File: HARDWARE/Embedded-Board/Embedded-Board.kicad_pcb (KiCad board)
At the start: 2 copper layers, 80 x 60 mm, 81 parts, among them J1 AD7265X, J11 USB_C_Receptacle_USB2.0, J2 POWER-pins, J3 Conn_02x20_Odd_Even, J4 AD7341, J5 I2C comm, J6 GPIO PINS, Q1 MMUN2133LT1G, SW1 SW_Push, SW2 RotaryEncoder_Switch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

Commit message: small update
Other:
- board text added: "Harvey McBurney Ryan Najami Nicolas Viale"
- board text removed: "Harvet McBurney Ryan Namaji Nicolas Viale"

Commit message: Final PCB version
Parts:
- added D4: WHITE-LED, LED_SMD:LED_1206_3216Metric, F.Cu at (173.2, 88.6)
- added D5: IR_LED, LED_SMD:LED_0805_2012Metric, F.Cu at (187.1, 88.6)
- added D6: UV_LED, LED_SMD:LED_PLCC_2835, F.Cu at (180.2, 76.7)
- added G***: LOGO, test:uofg-8mm, B.Cu at (180.2, 84.7)
- added J7: BOARD->LED, Connector_PinHeader_2.54mm:PinHeader_1x03_P2.54mm_Vertical, F.Cu at (152.8, 68.4)
- added J8: LED->BOARD, Connector_PinHeader_2.54mm:PinHeader_1x03_P2.54mm_Vertical, F.Cu at (203.4, 68.4)
- added JP1: VBUS-5V, Jumper:SolderJumper-2_P1.3mm_Open_TrianglePad1.0x1.5mm, F.Cu at (84.3, 96.7)
- added JP2: OUT-5V, Jumper:SolderJumper-2_P1.3mm_Bridged_Pad1.0x1.5mm, F.Cu at (110.8, 100.2)
- added Q3: Q_NPN_BEC, Package_TO_SOT_THT:TO-92_Wide, B.Cu at (169.9, 95.6)
- added Q4: Q_NPN_BEC, Package_TO_SOT_THT:TO-92_Wide, B.Cu at (184.8, 95.9)
- added Q5: Q_NPN_BEC, Package_TO_SOT_THT:TO-92_Wide, B.Cu at (182.7, 71.4)
- added R23: 10k, Resistor_THT:R_Axial_DIN0411_L9.9mm_D3.6mm_P12.70mm_Horizontal, B.Cu at (186.6, 102.9)
- added R24: 10k, Resistor_THT:R_Axial_DIN0411_L9.9mm_D3.6mm_P12.70mm_Horizontal, B.Cu at (198.4, 91.7)
- added R25: 10k, Resistor_THT:R_Axial_DIN0411_L9.9mm_D3.6mm_P12.70mm_Horizontal, B.Cu at (192.8, 59.4)
- added R26: 470, Resistor_THT:R_Axial_DIN0411_L9.9mm_D3.6mm_P12.70mm_Horizontal, B.Cu at (165.2, 110.9)
- added R27: 470, Resistor_THT:R_Axial_DIN0411_L9.9mm_D3.6mm_P12.70mm_Horizontal, B.Cu at (194.6, 111.2)
- added R28: 470, Resistor_THT:R_Axial_DIN0411_L9.9mm_D3.6mm_P12.70mm_Horizontal, B.Cu at (172.3, 59.0)
- added REF**: Fiducial_1mm_Mask3mm, Fiducial:Fiducial_1mm_Mask3mm, F.Cu at (197.1, 116.6)
- added REF**: TestPoint, user:1.3mm_Test_Point, F.Cu at (202.2, 51.6)
- added REF**: Fiducial_1mm_Mask3mm, Fiducial:Fiducial_1mm_Mask3mm, F.Cu at (83.2, 52.7)
- added REF**: MountingHole_3.2mm_M3_ISO14580_Pad, MountingHole:MountingHole_3.2mm_M3_ISO14580_Pad, F.Cu at (185.2, 62.1)
- added REF**: TestPoint, user:1.3mm_Test_Point, F.Cu at (202.1, 117.7)
- added REF**: MountingHole_3.2mm_M3_ISO14580_Pad, MountingHole:MountingHole_3.2mm_M3_ISO14580_Pad, F.Cu at (135.2, 62.1)
- added REF**: MountingHole_3.2mm_M3_ISO14580_Pad, MountingHole:MountingHole_3.2mm_M3_ISO14580_Pad, F.Cu at (163.8, 92.2)
- added REF**: TestPoint, user:1.3mm_Test_Point, F.Cu at (78.2, 51.6)
- added REF**: Fiducial_1mm_Mask3mm, Fiducial:Fiducial_1mm_Mask3mm, F.Cu at (197.1, 52.7)
- added REF**: MountingHole_3.2mm_M3_ISO14580_Pad, MountingHole:MountingHole_3.2mm_M3_ISO14580_Pad, F.Cu at (185.2, 110.3)
- added REF**: MountingHole_3.2mm_M3_ISO14580_Pad, MountingHole:MountingHole_3.2mm_M3_ISO14580_Pad, F.Cu at (113.8, 92.2)
- added REF**: TestPoint, user:1.3mm_Test_Point, F.Cu at (78.2, 117.7)
- added REF**: Fiducial_1mm_Mask3mm, Fiducial:Fiducial_1mm_Mask3mm, F.Cu at (83.2, 116.6)
- added REF**: MountingHole_3.2mm_M3_ISO14580_Pad, MountingHole:MountingHole_3.2mm_M3_ISO14580_Pad, F.Cu at (135.2, 110.3)
- C2, C3, C5: footprint Capacitor_SMD:C_0603_1608Metric -> Capacitor_SMD:C_0805_2012Metric
- C6: footprint Capacitor_SMD:C_0805_2012Metric -> Capacitor_SMD:C_1206_3216Metric
- moved J6 7.50 mm to (145.3, 57.0)
- moved TP7 2.44 mm to (119.7, 58.6)
- moved TP6 2.31 mm to (116.8, 58.5)
- moved R13 1.37 mm to (85.8, 58.9), turned to 0 degrees
- moved R14 1.30 mm to (86.5, 62.5), turned to 180 degrees
- moved R6 1.05 mm to (92.5, 77.4)
- moved R8 1.05 mm to (92.5, 79.3)
- moved R9 1.05 mm to (100.1, 77.5)
- moved U1 1.05 mm to (96.3, 78.4)
- moved C6 0.90 mm to (118.4, 97.3)
- moved C2 0.80 mm to (100.3, 79.7)
- moved R17 0.50 mm to (87.7, 94.1)
- moved C3 0.40 mm to (89.6, 93.9)
- moved C5 0.32 mm to (113.8, 97.5)
- moved C19 0.10 mm to (108.2, 56.4)
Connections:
- R18 pad 2: +5V -> Net-(JP2-A)
- U3 pad 36: SENSOR-INT -> unconnected-(U3-GPIO24-Pad36)
- U3 pad 37: SENSOR-RST -> unconnected-(U3-GPIO25-Pad37)
- U3 pad 8: unconnected-(U3-GPIO6-Pad8) -> SENSOR-INT
- U3 pad 9: unconnected-(U3-GPIO7-Pad9) -> SENSOR-RST
- U4 pad 1: +5V -> Net-(JP2-A)
- U4 pad 15: +5V -> Net-(JP2-A)
- U4 pad 16: +5V -> Net-(JP2-A)
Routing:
- net +3.3V: track 0.00 -> 323.8 mm, vias 0 -> 14
- net +VBAT: track 0.00 -> 102.3 mm, vias 0 -> 4
- net +5V: track 0.00 -> 93.5 mm, vias 0 -> 3
- net LED-BOARD: track 0.00 -> 90.9 mm
- net VBUS: track 0.00 -> 88.9 mm, vias 0 -> 5
- net PUSH-SWITCH: track 0.00 -> 84.4 mm, vias 0 -> 2
- net ENC-PSH: track 0.00 -> 83.1 mm, vias 0 -> 4
- net Net-(SW3-B): track 0.00 -> 80.0 mm, vias 0 -> 4
- net SENSOR-SDA: track 0.00 -> 74.4 mm, vias 0 -> 1
- net SENSOR-RST: track 0.00 -> 71.7 mm, vias 0 -> 4
- net SENSOR-INT: track 0.00 -> 69.5 mm, vias 0 -> 1
- net SENSOR-SCL: track 0.00 -> 68.7 mm, vias 0 -> 1
- net ENC-B: track 0.00 -> 66.6 mm, vias 0 -> 3
- net ENC-A: track 0.00 -> 62.0 mm, vias 0 -> 4
- net Net-(D3-A): track 0.00 -> 60.0 mm, vias 0 -> 2
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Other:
- board size 80 x 60 mm -> 131.5 x 73.5 mm
- board text added: "3.3V"
- board text added: "5V"
- board text added: "CNC"
- board text added: "Drawn by Nicolas Viale"
- board text added: "ENG5026 Design Special Topic LED Board"
- board text added: "GPIO PINS"
- board text added: "IR_LED"
- board text added: "LED"
- board text added: "Schematic & PCB"
- board text added: "Spectrometer Board LED board v1.0 Apr. 2025"
- board text added: "Spectrometer Board v1.0 Apr. 2025"
- board text added: "UV_LED"
- board text added: "V-CUT"
- board text added: "VBUS"
- board text added: "WHITE_LED"
- board text added: "~10k"
- board text added: "~470"
- board text removed: "RP2040 GPIO PINS"
- board text removed: "Schematic & PCB drawn by Nicolas Viale"

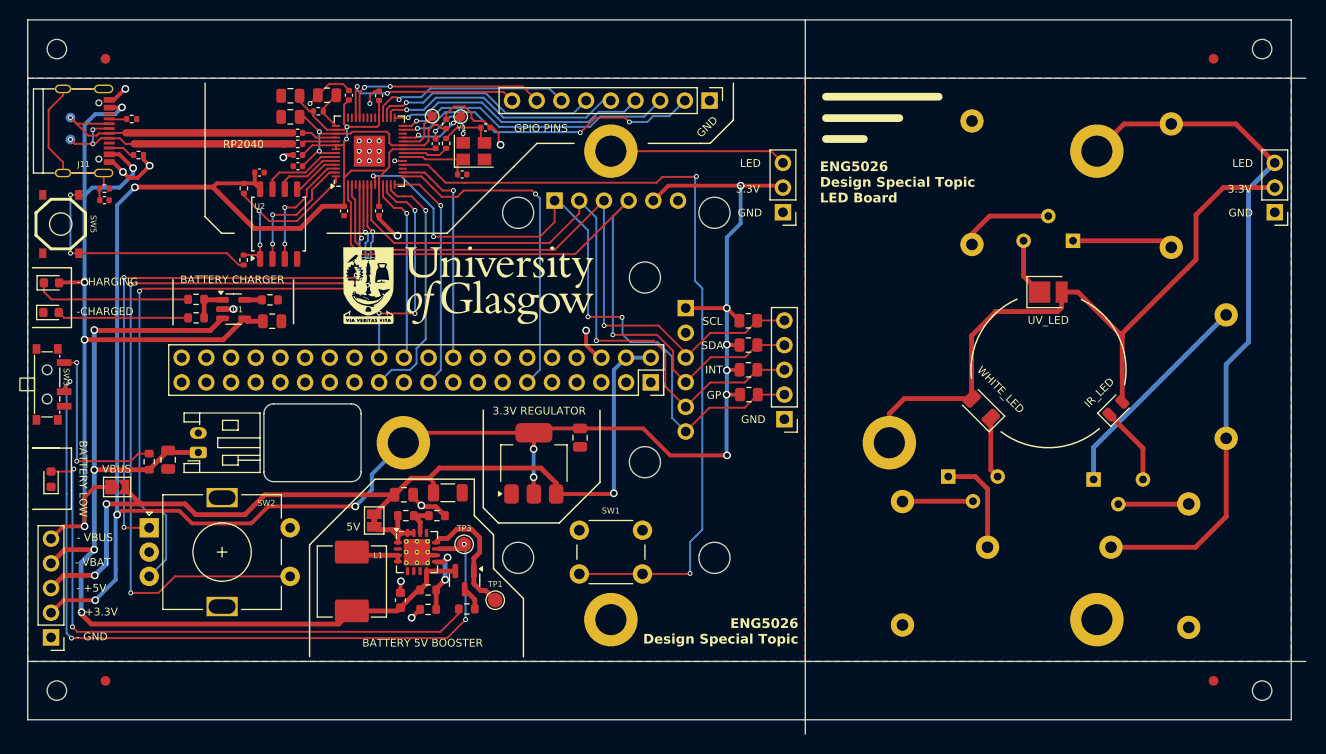
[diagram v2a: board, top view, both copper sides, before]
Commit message: Splitting the Embedded & LED PCBs
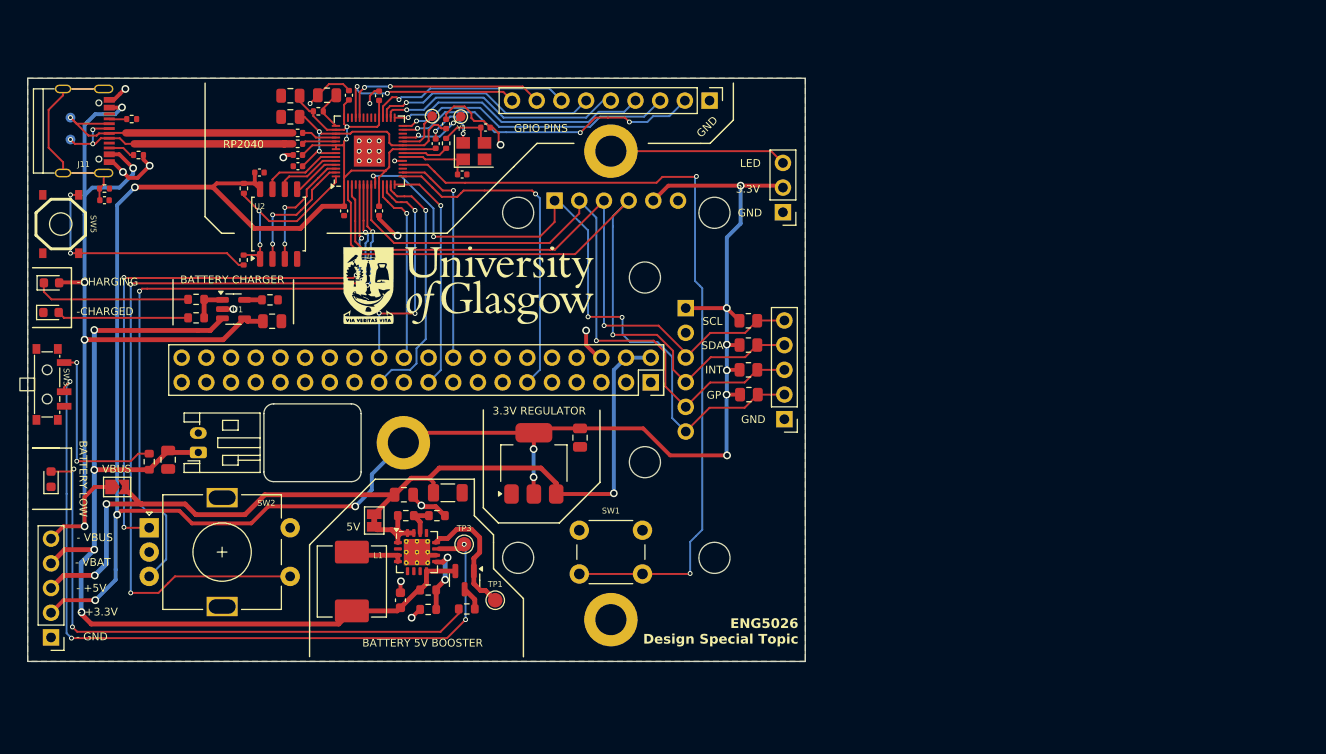
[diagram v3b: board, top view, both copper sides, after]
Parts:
- removed D4: WHITE-LED, LED_SMD:LED_1206_3216Metric
- removed D5: IR_LED, LED_SMD:LED_0805_2012Metric
- removed D6: UV_LED, LED_SMD:LED_PLCC_2835
- removed the G*** at (180.2, 84.7)
- removed J8: LED->BOARD, Connector_PinHeader_2.54mm:PinHeader_1x03_P2.54mm_Vertical
- removed Q3, Q4, Q5: Q_NPN_BEC, Package_TO_SOT_THT:TO-92_Wide
- removed R23, R24, R25: 10k, Resistor_THT:R_Axial_DIN0411_L9.9mm_D3.6mm_P12.70mm_Horizontal
- removed R26, R27, R28: 470, Resistor_THT:R_Axial_DIN0411_L9.9mm_D3.6mm_P12.70mm_Horizontal
- removed the REF** at (197.1, 116.6)
- removed the REF** at (202.2, 51.6)
- removed the REF** at (83.2, 52.7)
- removed the REF** at (185.2, 62.1)
- removed the REF** at (202.1, 117.7)
- removed the REF** at (163.8, 92.2)
- removed the REF** at (78.2, 51.6)
- removed the REF** at (197.1, 52.7)
- removed the REF** at (185.2, 110.3)
- removed the REF** at (78.2, 117.7)
- removed the REF** at (83.2, 116.6)
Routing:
- net LED-BOARD: track 90.9 -> 18.2 mm
- net +3.3V: track 323.8 -> 253.4 mm
- net Net-(Q4-B): track 22.6 -> 0.00 mm
- net Net-(Q3-B): track 10.6 -> 0.00 mm
- net Net-(Q5-B): track 10.4 -> 0.00 mm
- net Net-(Q5-E): track 9.70 -> 0.00 mm
- net Net-(D5-K): track 8.10 -> 0.00 mm
- net Net-(Q3-E): track 7.26 -> 0.00 mm
- net Net-(Q4-E): track 7.26 -> 0.00 mm
- net Net-(D4-K): track 6.33 -> 0.00 mm
- net Net-(D6-K): track 5.96 -> 0.00 mm
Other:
- board size 131.5 x 73.5 mm -> 80 x 60 mm
- board text removed: "ENG5026 Design Special Topic LED Board"
- board text removed: "IR_LED"
- board text removed: "Spectrometer Board LED board v1.0 Apr. 2025"
- board text removed: "UV_LED"
- board text removed: "V-CUT"
- board text removed: "WHITE_LED"
- board text removed: "~10k"
- board text removed: "~470"
